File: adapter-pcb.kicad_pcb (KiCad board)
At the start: 2 copper layers, 90.2 x 95.9 mm, 34 parts, among them J1 SS5-80-3.50-L-D-K-TR, J2 DM3BT-DSF-PEJS, J3 Conn_02x05_Odd_Even, U1 TXS0102QDCURQ1, U2 LTC4300A-1IMS8_PBF, U3 TXS02612RTWR

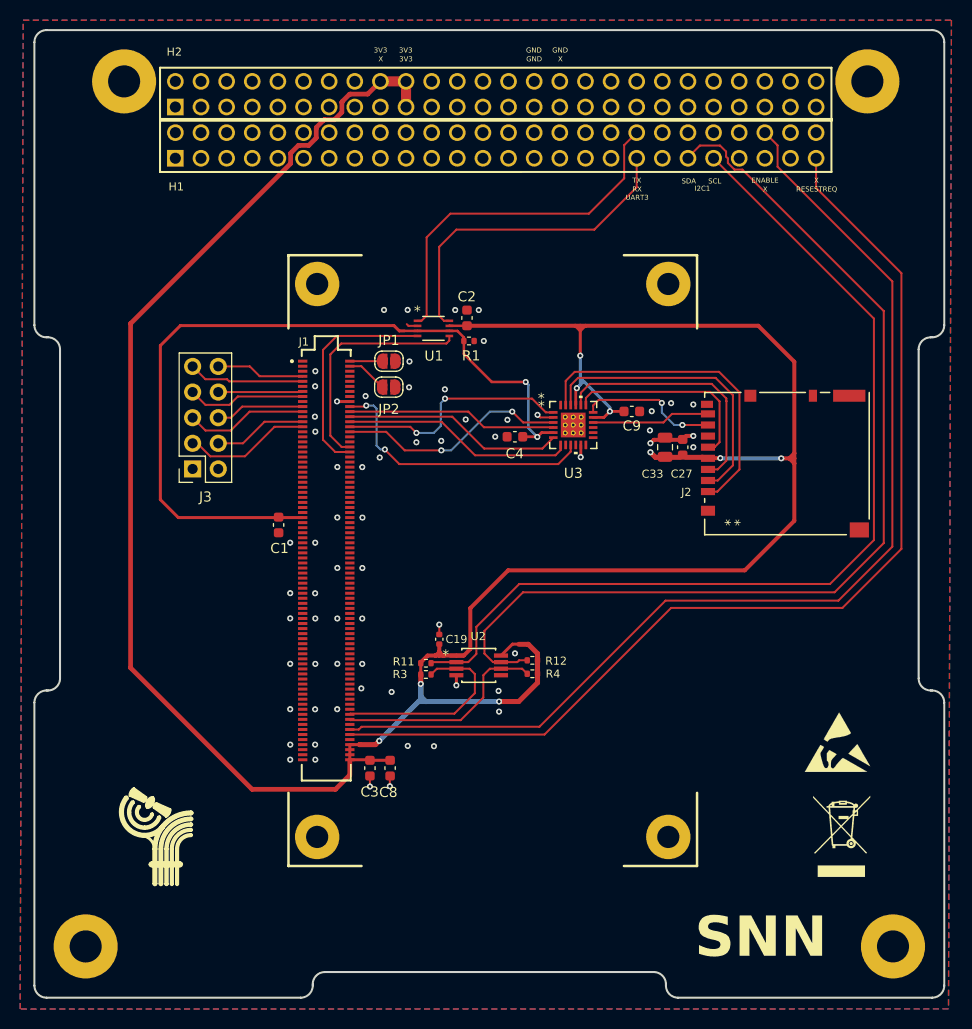
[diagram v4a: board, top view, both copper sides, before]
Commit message: Rerouted 3V3 trace
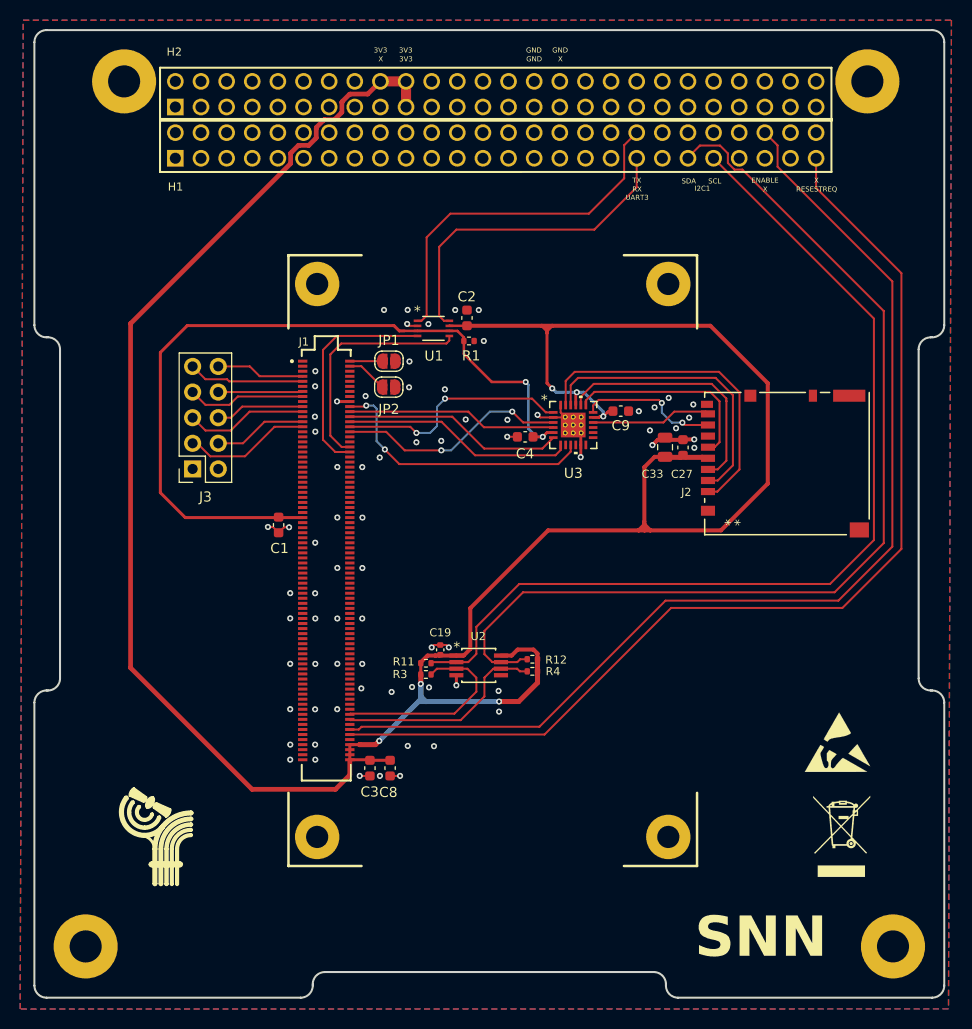
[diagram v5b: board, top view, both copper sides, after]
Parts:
- moved C9 1.10 mm to (163.5, 84.3)
- moved C19 1.05 mm to (145.6, 107.9)
- moved C4 1.02 mm to (154.1, 86.8)
- moved R4 0.24 mm to (154.8, 110.0)
- moved R12 0.11 mm to (154.8, 108.8)
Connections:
- U3 pad 25: unconnected-(U3-EPAD-Pad25) -> GND
- U3 pad V: (no net) -> GND
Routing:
- net +3V3: track 276.9 -> 264.4 mm, vias 9 -> 6
- net GND: track 14.0 -> 23.1 mm, vias 65 -> 74
- net +1V8: track 79.6 -> 78.3 mm

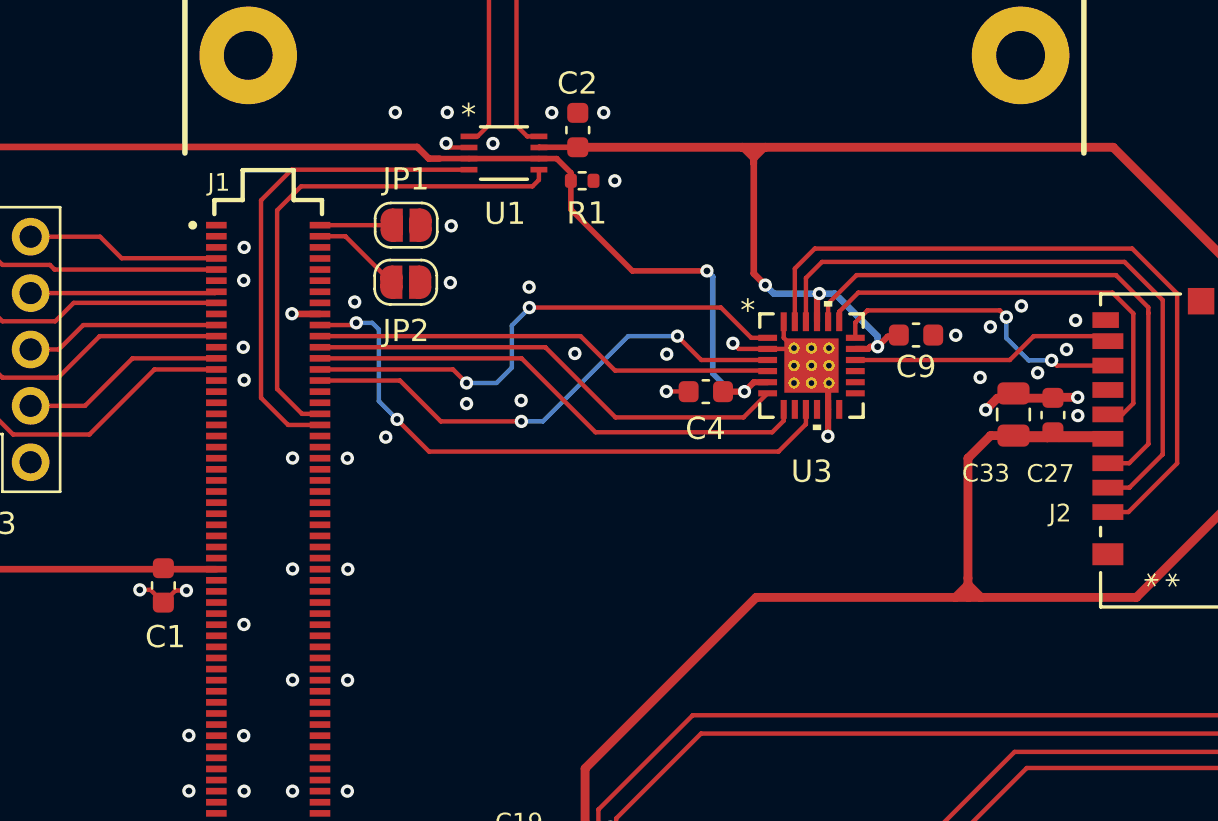
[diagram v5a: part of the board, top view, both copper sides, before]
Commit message: moved vias farther from pads
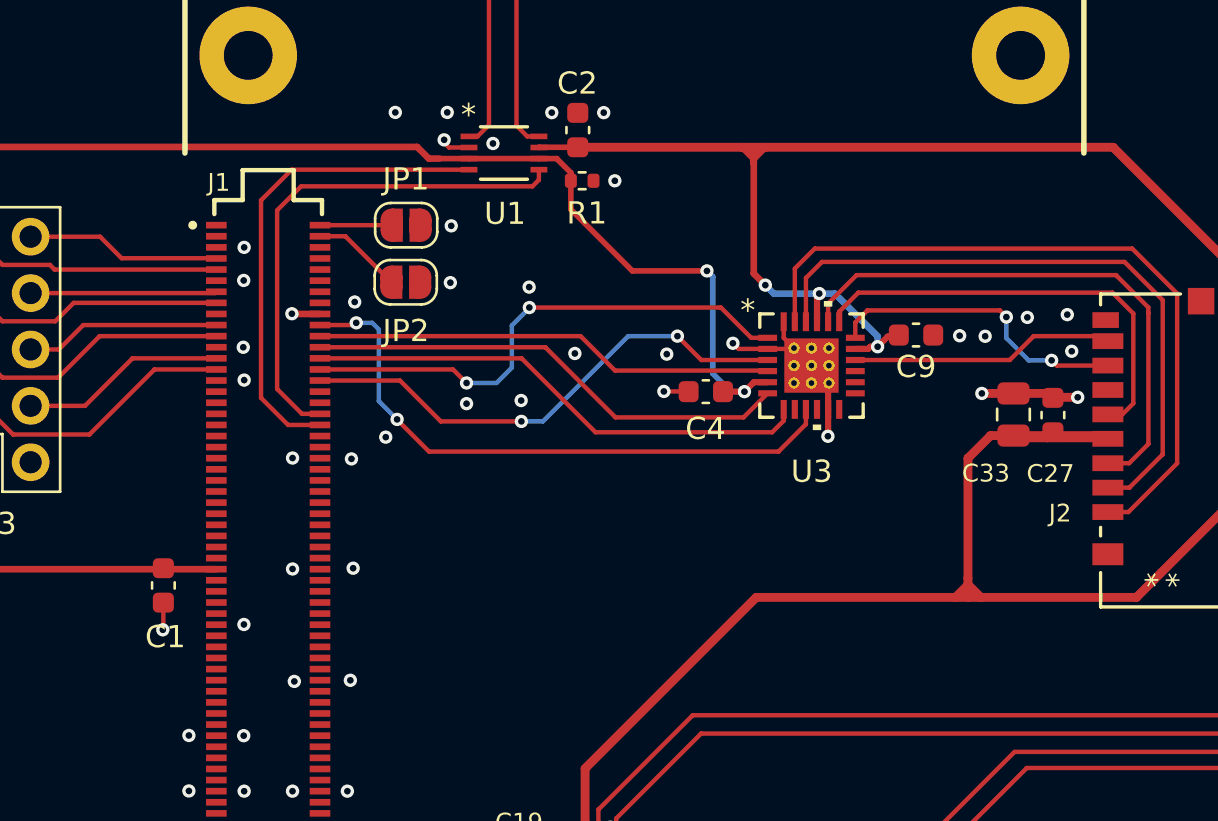
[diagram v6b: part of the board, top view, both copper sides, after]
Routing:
- net GND: track 23.1 -> 22.1 mm, vias 74 -> 70

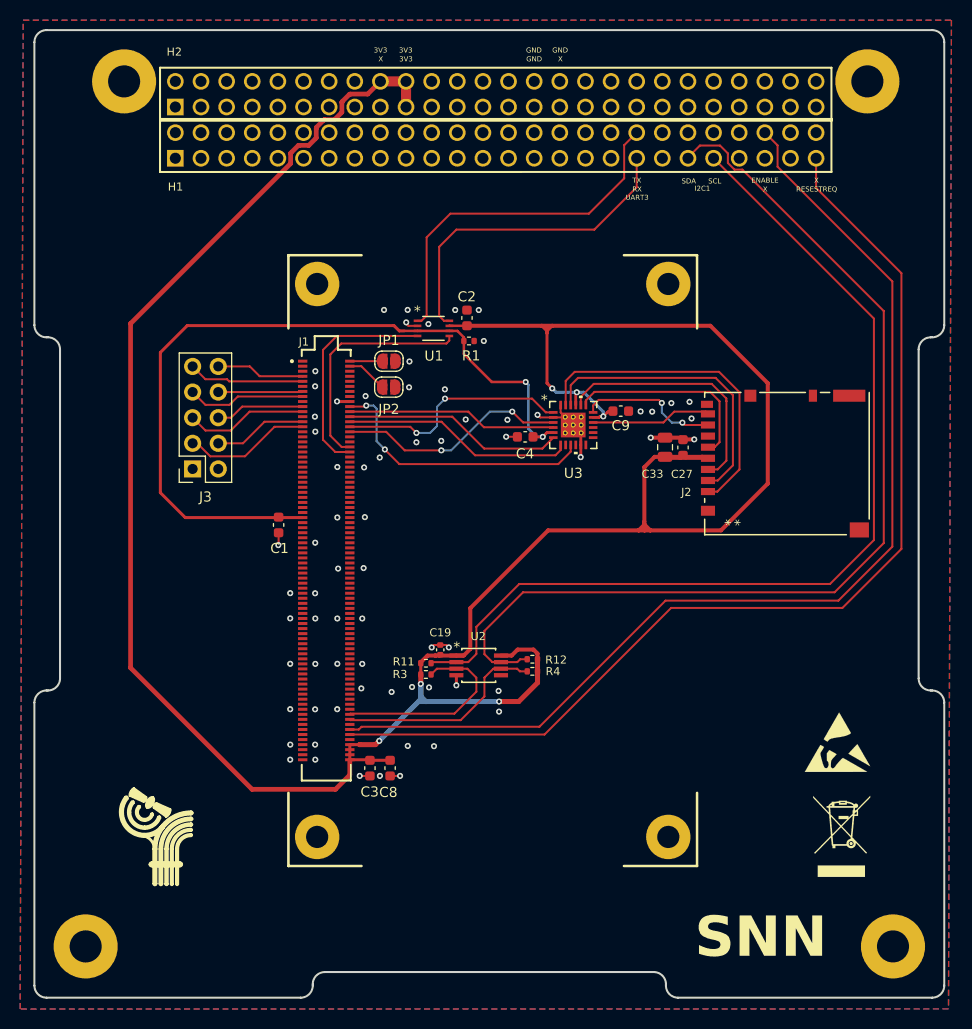
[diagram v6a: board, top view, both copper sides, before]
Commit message: Added pcb files for ethernet breakout board
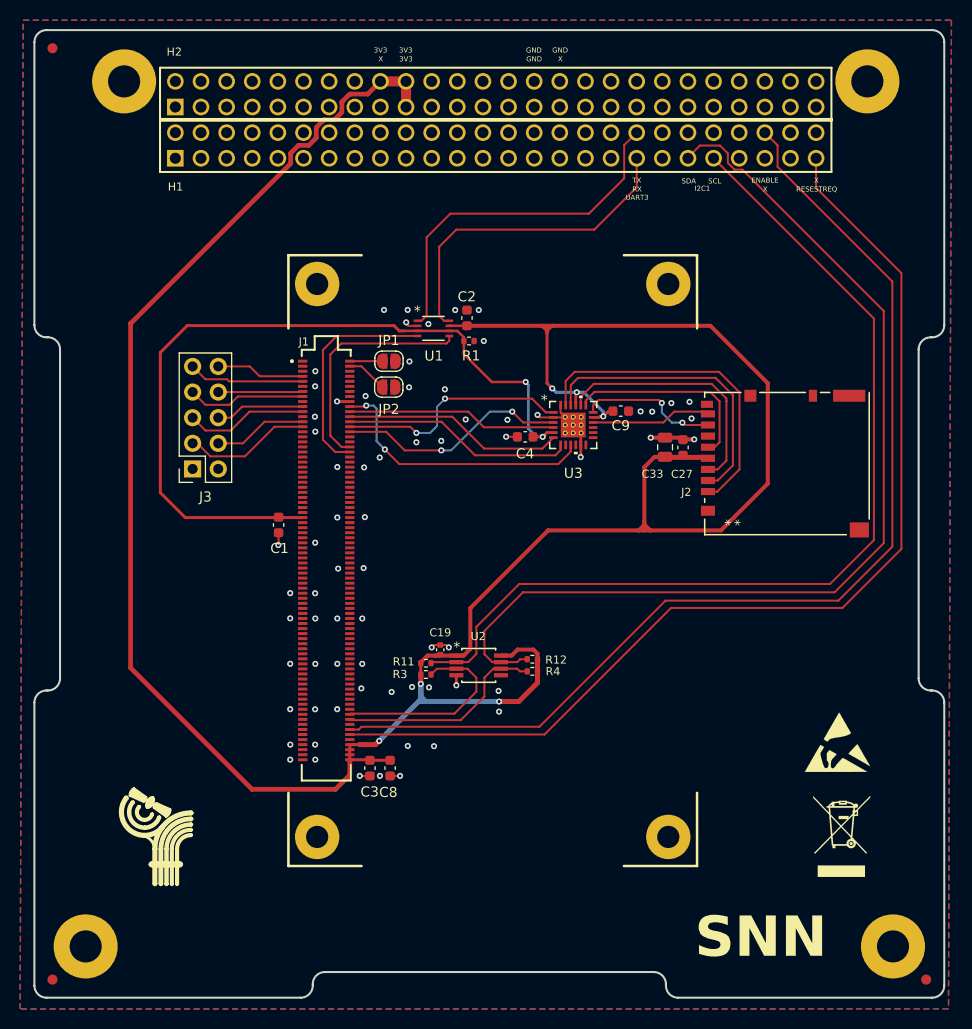
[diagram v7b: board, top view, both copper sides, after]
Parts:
- added ?: , , F.Cu at (107.2, 48.3)
- added REF**: Fiducial_1mm_Mask2mm, Fiducial:Fiducial_1mm_Mask2mm, F.Cu at (193.8, 140.6)
- added REF**: Fiducial_1mm_Mask2mm, Fiducial:Fiducial_1mm_Mask2mm, F.Cu at (107.2, 140.6)
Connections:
- U3 pad V: GND -> (no net)

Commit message: Updated BOM and added fiducials
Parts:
- C8: value 1uF -> 1u
